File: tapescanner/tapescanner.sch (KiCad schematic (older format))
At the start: 43 parts, among them J0 USB_B, J2 AVR-ISP-10, M0 Motor_DC, Q0 TEPT5600, Q1 TEPT5600, Q10 MJE13007G, Q2 TEPT5600, Q3 TEPT5600, Q4 TEPT5600, Q5 TEPT5600, Q6 TEPT5600, Q7 TEPT5600, Q8 TEPT5600, Q9 TEPT5600, SW0 SW_Push, U0 ATmega328P-PU, U1 FT232RL

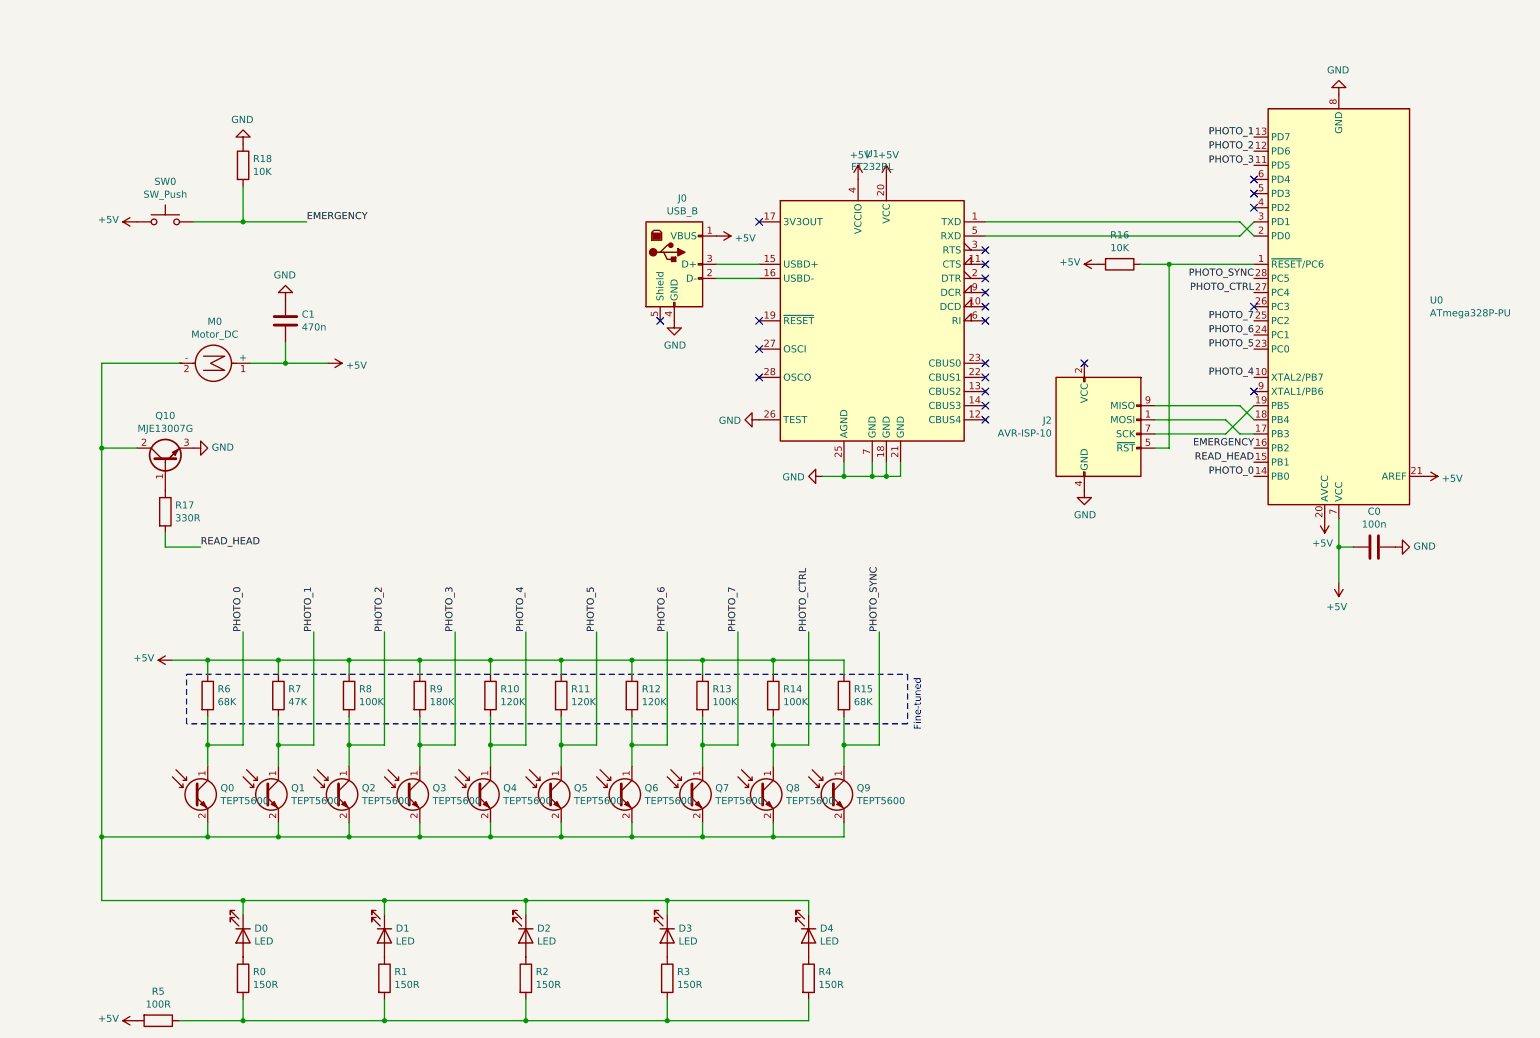
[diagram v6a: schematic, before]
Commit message: Include EM212 board in schematic
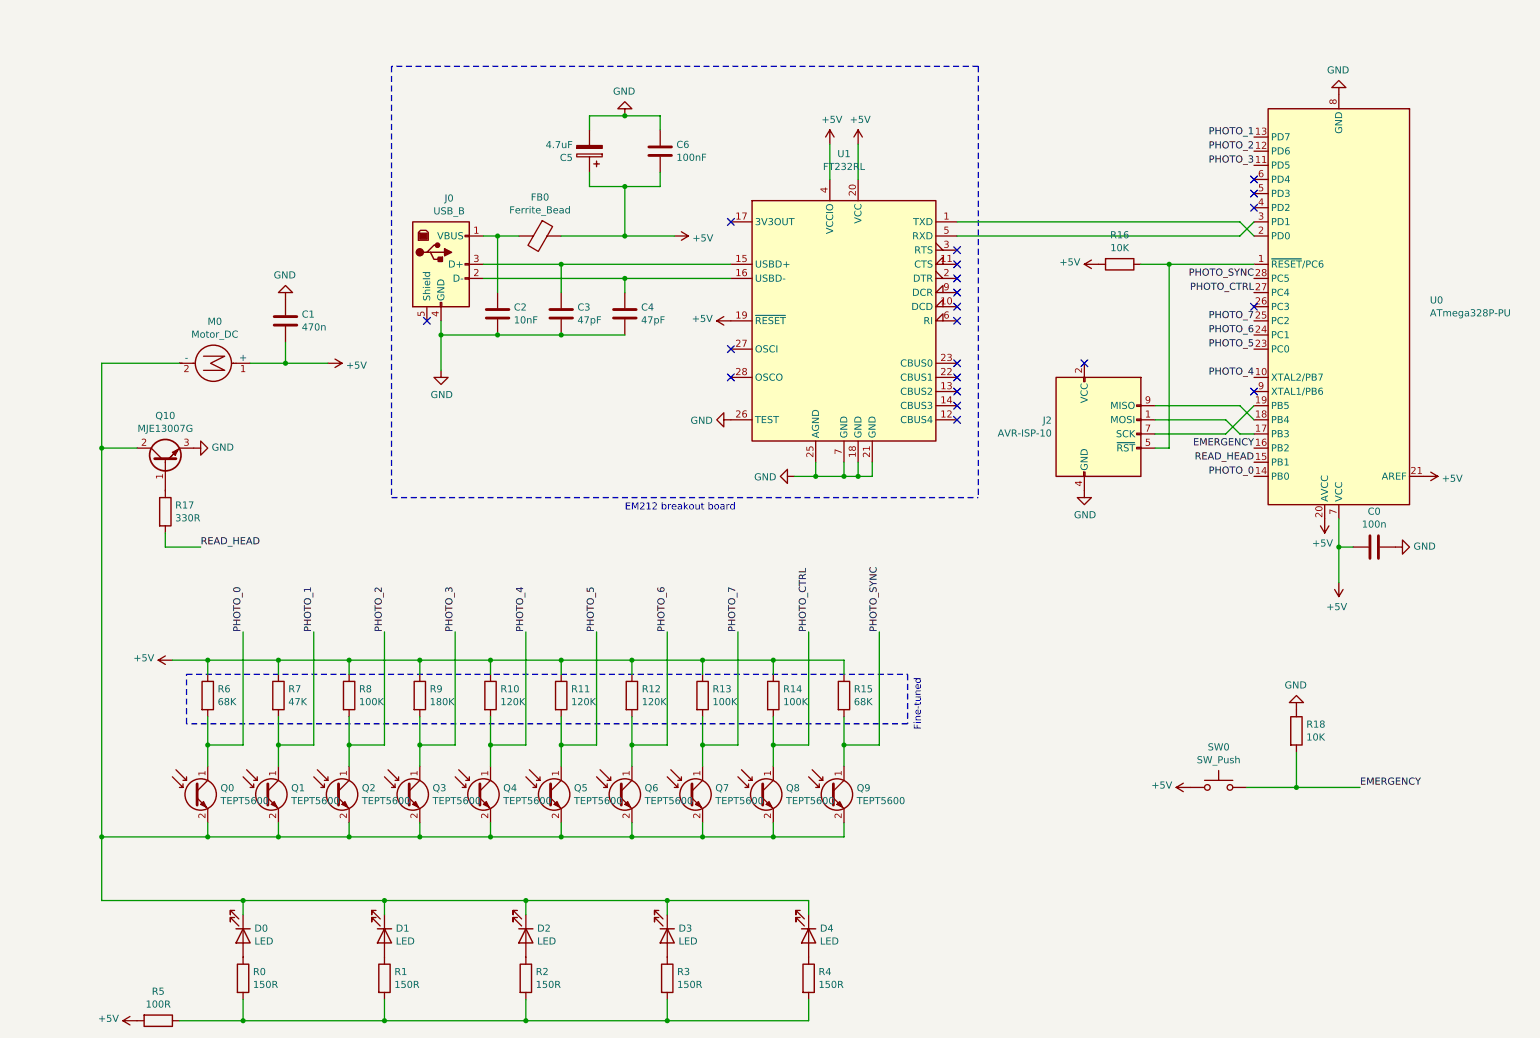
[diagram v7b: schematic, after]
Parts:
- added C2: 10nF, symbol Device:C
- added C3, C4: 47pF, symbol Device:C
- added C5: 4.7uF, symbol Device:CP
- added C6: 100nF, symbol Device:C
- added FB0: Ferrite_Bead, symbol Device:Ferrite_Bead
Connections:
- net +5V: now also U1.19 (~RESET~), C5.1, C6.2, FB0.1; no longer J0.1 (VBUS)
- net GND: now also C2.2, C3.2, C4.2, C5.2, C6.1
- net at J0.3 (D+), U1.15 (USBD+): now also C3.1
- net at J0.2 (D-), U1.16 (USBD-): now also C4.1
- new net: C2.1, FB0.2, J0.1 (VBUS)
- no-connect marks 22 -> 21
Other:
- note added: "EM212 breakout board"
- moved on the sheet: J0, R18, SW0, U1

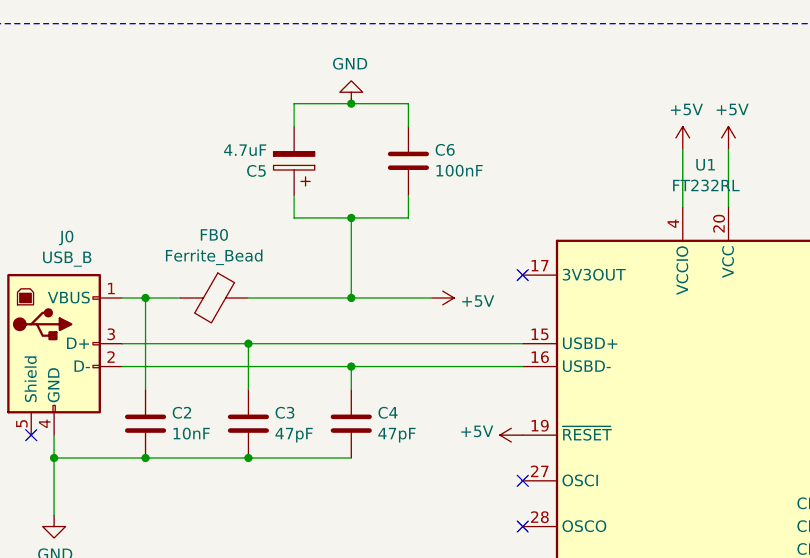
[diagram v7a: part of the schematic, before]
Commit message: Add missing power flag
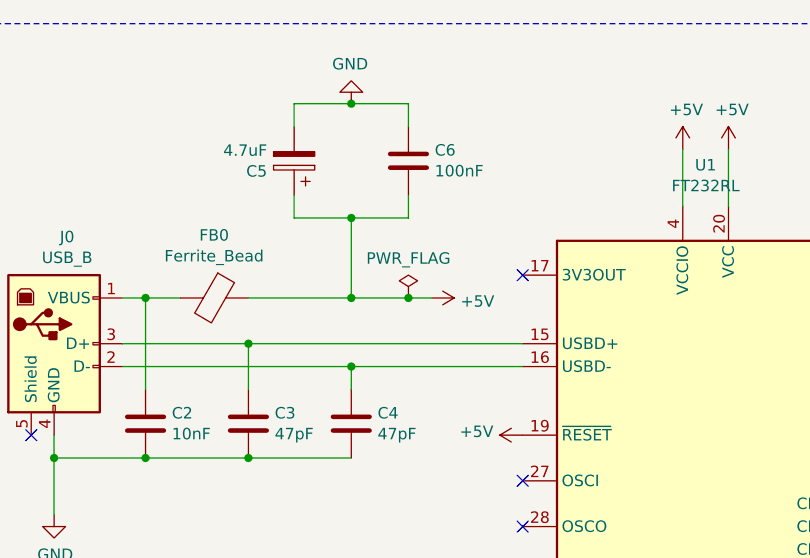
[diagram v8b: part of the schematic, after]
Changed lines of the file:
@@
 	4650 2350 4650 2250
 $Comp
-L power:+5V #PWR?
+L power:+5V #PWR0121
 U 1 1 6083295D
 P 5400 2550
-F 0 "#PWR?" H 5400 2400 50  0001 C CNN
+F 0 "#PWR0121" H 5400 2400 50  0001 C CNN
 F 1 "+5V" V 5415 2678 50  0000 L CNN
 F 2 "" H 5400 2550 50  0001 C CNN
@@
 	4900 1100 4650 1100
 $Comp
-L power:GND #PWR?
+L power:GND #PWR0122
 U 1 1 608701A5
 P 4650 1100
-F 0 "#PWR?" H 4650 850 50  0001 C CNN
+F 0 "#PWR0122" H 4650 850 50  0001 C CNN
 F 1 "GND" H 4655 927 50  0000 C CNN
 F 2 "" H 4650 1100 50  0001 C CNN
@@
 Connection ~ 4650 1950
 Wire Wire Line
-	4650 1950 5000 1950
+	4650 1950 4900 1950
 Wire Wire Line
 	3350 2550 3350 2650
@@
 Connection ~ 3750 2650
 Connection ~ 3350 2650
-Wire Wire Line
-	3350 2650 3350 2900
 Wire Wire Line
 	6100 1300 6100 1550
@@
 	1    0    0    -1
 $EndComp
+$Comp
+L power:PWR_FLAG #FLG0101
+U 1 1 60A051E1
+P 4900 1950
+F 0 "#FLG0101" H 4900 2025 50  0001 C CNN
+F 1 "PWR_FLAG" H 4900 2123 50  0000 C CNN
+F 2 "" H 4900 1950 50  0001 C CNN
+F 3 "~" H 4900 1950 50  0001 C CNN
+	1    4900 1950
+	1    0    0    -1
+$EndComp
+Connection ~ 4900 1950
+Wire Wire Line
+	4900 1950 5000 1950
+Wire Wire Line
+	3350 2650 3350 2900
 $EndSCHEMATC
